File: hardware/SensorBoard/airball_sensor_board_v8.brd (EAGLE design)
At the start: 88.9 x 38.1 mm, 65 parts, among them IC1 CP2102, J2 QWIIC_RIGHT_ANGLE, J5 105450-0101, T1 BC846, T2 BC846, U1 BQ24075, U2 BQ27441-G1, U3 BMP390, U4 ESP-WROOM-32, U7 SP0503BAHT

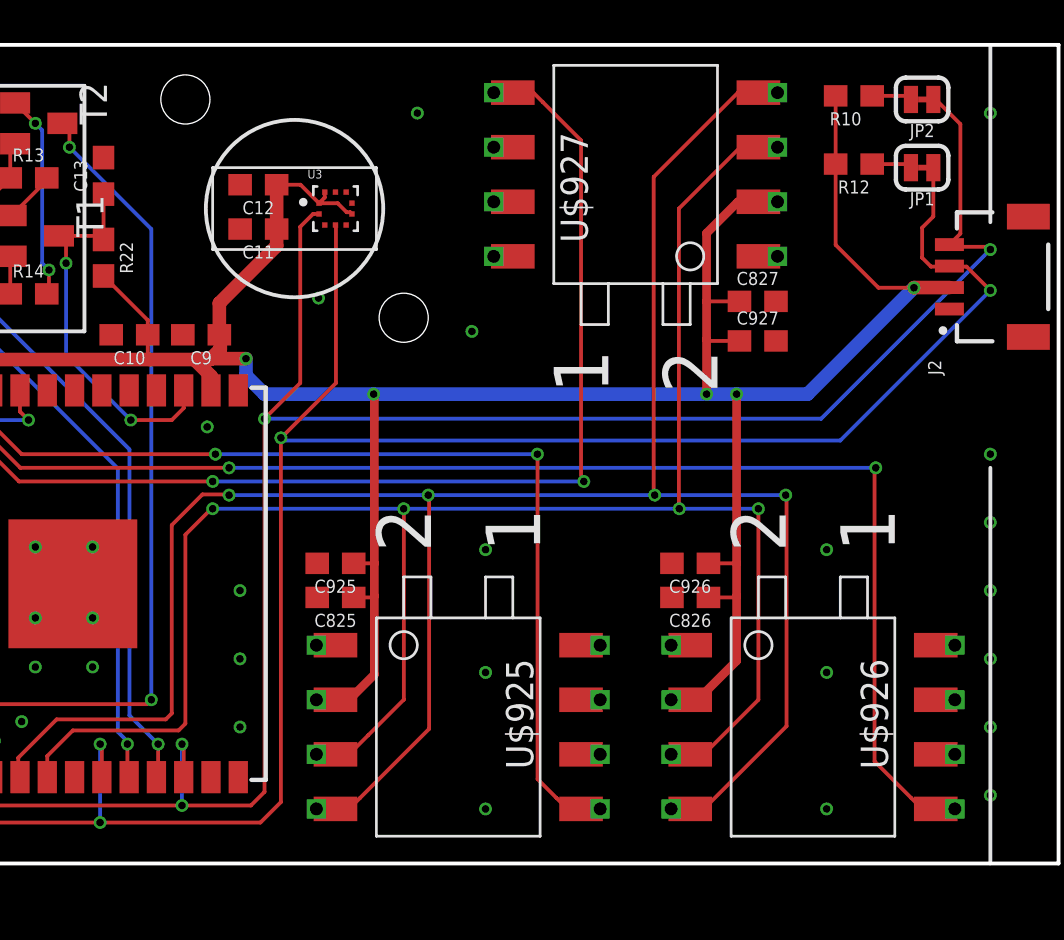
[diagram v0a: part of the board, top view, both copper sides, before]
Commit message: Changed location of barometer and mounting.
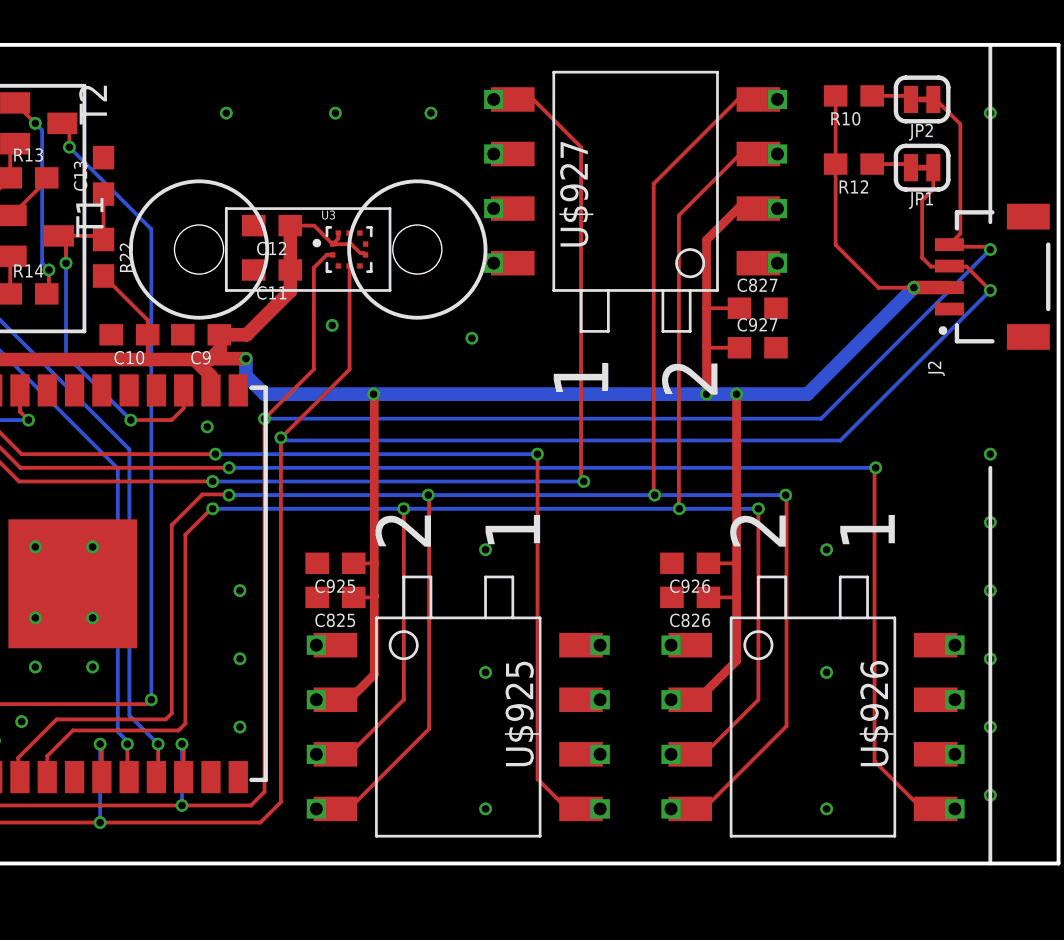
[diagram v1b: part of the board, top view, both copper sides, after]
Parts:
- moved C11 2.01 mm to (52.3, 27.6)
- moved U3 2.01 mm to (55.9, 28.6)
- moved C12 2.01 mm to (52.3, 29.7)
- moved U$927 0.32 mm to (69.2, 31.8)
- moved C827 0.32 mm to (74.9, 25.8)
- moved C927 0.32 mm to (74.9, 24.0)
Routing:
- net SDA: track 120.5 -> 118.9 mm
- net SCL: track 120.5 -> 118.8 mm
- net VCC: track 184.5 -> 183.2 mm
